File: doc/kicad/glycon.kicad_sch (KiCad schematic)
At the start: 17 parts, among them J1 2x20 Header, J2 USB_B, SW1 SW_Push, U0 Z80CPU, U1 628128_DIP32_SSOP32, U2 SST39SF010, U3 74HC32, U4 74HC86, X1 ACO-6.00MHz

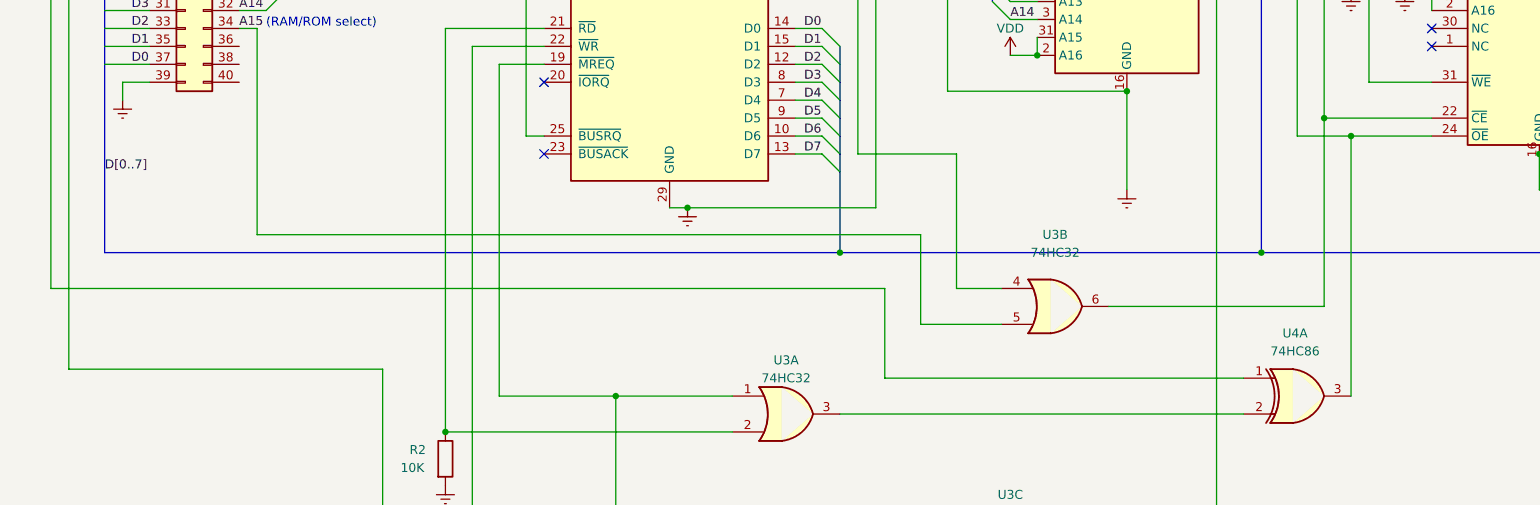
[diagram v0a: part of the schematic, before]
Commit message: add xor gates between coproc header and OE, ROM WE
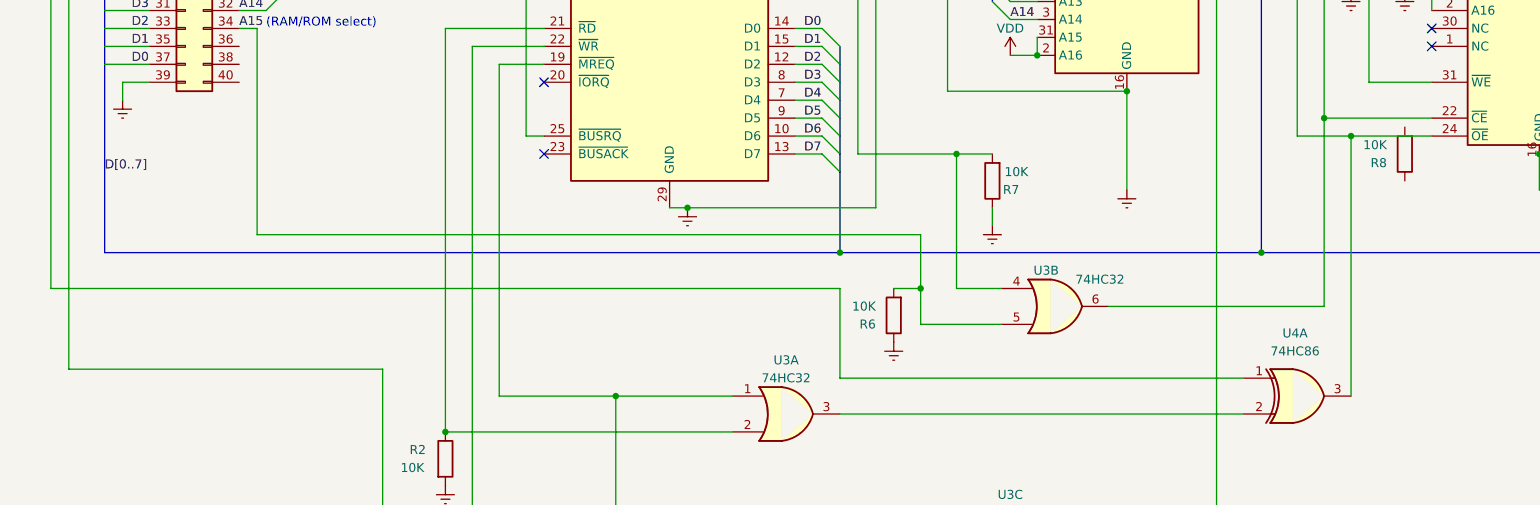
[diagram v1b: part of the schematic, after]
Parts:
- added R6, R7, R8: 10K, Resistor_THT:R_Axial_DIN0204_L3.6mm_D1.6mm_P5.08mm_Horizontal, symbol Device:R
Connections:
- net A15: now also R6.2
- net Earth: now also R6.1, R7.1
- net at U0.5 (A15), U3.4: now also R7.2
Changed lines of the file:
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@@
   (junction (at 114.3 114.3) (diameter 0) (color 0 0 0 0)
   )
+  (junction (at 147.32 125.73) (diameter 0) (color 0 0 0 0)
+  )
   (junction (at 111.76 38.1) (diameter 0) (color 0 0 0 0)
   )
@@
   )
   (junction (at 234.95 35.56) (diameter 0) (color 0 0 0 0)
+  )
+  (junction (at 152.4 106.68) (diameter 0) (color 0 0 0 0)
   )
   (junction (at 91.44 76.2) (diameter 0) (color 0 0 0 0)
@@
     (stroke (width 0) (type default) (color 0 0 0 0))
   )
-  (wire (pts (xy 147.32 118.11) (xy 147.32 130.81))
+  (wire (pts (xy 147.32 118.11) (xy 147.32 125.73))
     (stroke (width 0) (type default) (color 0 0 0 0))
   )
@@
     (stroke (width 0) (type default) (color 0 0 0 0))
   )
-  (wire (pts (xy 142.24 138.43) (xy 142.24 125.73))
+  (wire (pts (xy 135.89 138.43) (xy 135.89 125.73))
     (stroke (width 0) (type default) (color 0 0 0 0))
   )
@@
     (stroke (width 0) (type default) (color 0 0 0 0))
   )
-  (wire (pts (xy 193.04 138.43) (xy 142.24 138.43))
+  (wire (pts (xy 193.04 138.43) (xy 135.89 138.43))
     (stroke (width 0) (type default) (color 0 0 0 0))
   )
@@
     (stroke (width 0) (type default) (color 0 0 0 0))
   )
+  (wire (pts (xy 157.48 114.3) (xy 157.48 116.84))
+    (stroke (width 0) (type default) (color 0 0 0 0))
+  )
   (wire (pts (xy 250.19 63.5) (xy 254 63.5))
     (stroke (width 0) (type default) (color 0 0 0 0))
@@
     (stroke (width 0) (type default) (color 0 0 0 0))
   )
+  (wire (pts (xy 152.4 106.68) (xy 152.4 125.73))
+    (stroke (width 0) (type default) (color 0 0 0 0))
+  )
   (wire (pts (xy 160.02 80.01) (xy 163.83 80.01))
     (stroke (width 0) (type default) (color 0 0 0 0))
@@
     (stroke (width 0) (type default) (color 0 0 0 0))
   )
+  (wire (pts (xy 143.51 125.73) (xy 147.32 125.73))
+    (stroke (width 0) (type default) (color 0 0 0 0))
+  )
   (wire (pts (xy 91.44 60.96) (xy 93.98 60.96))
     (stroke (width 0) (type default) (color 0 0 0 0))
@@
     (stroke (width 0) (type default) (color 0 0 0 0))
   )
+  (wire (pts (xy 147.32 125.73) (xy 147.32 130.81))
+    (stroke (width 0) (type default) (color 0 0 0 0))
+  )
   (wire (pts (xy 50.8 86.36) (xy 54.61 86.36))
     (stroke (width 0) (type default) (color 0 0 0 0))
@@
     (stroke (width 0) (type default) (color 0 0 0 0))
   )
-  (wire (pts (xy 152.4 125.73) (xy 152.4 106.68))
-    (stroke (width 0) (type default) (color 0 0 0 0))
-  )
   (bus (pts (xy 57.15 73.66) (xy 57.15 76.2))
     (stroke (width 0) (type default) (color 0 0 0 0))
@@
     (stroke (width 0) (type default) (color 0 0 0 0))
   )
+  (wire (pts (xy 152.4 106.68) (xy 157.48 106.68))
+    (stroke (width 0) (type default) (color 0 0 0 0))
+  )
   (bus (pts (xy 213.36 55.88) (xy 213.36 53.34))
     (stroke (width 0) (type default) (color 0 0 0 0))
@@
     (stroke (width 0) (type default) (color 0 0 0 0))
   )
-  (wire (pts (xy 142.24 125.73) (xy 24.13 125.73))
+  (wire (pts (xy 135.89 125.73) (xy 24.13 125.73))
     (stroke (width 0) (type default) (color 0 0 0 0))
   )
@@
   (label "A13" (at 160.02 85.09 0)
     (effects (font (size 1.27 1.27)) (justify left bottom))
+  )
+  (symbol (lib_id "power:Earth") (at 157.48 116.84 0) (unit 1)
+    (in_bom yes) (on_board yes) (fields_autoplaced)
+    (property "Reference" "#PWR09" (id 0) (at 157.48 123.19 0)
+      (effects (font (size 1.27 1.27)) hide)
+    )
+    (property "Value" "Earth" (id 1) (at 157.48 120.65 0)
+      (effects (font (size 1.27 1.27)) hide)
+    )
+    (property "Footprint" "" (id 2) (at 157.48 116.84 0)
+      (effects (font (size 1.27 1.27)) hide)
+    )
+    (property "Datasheet" "~" (id 3) (at 157.48 116.84 0)
+      (effects (font (size 1.27 1.27)) hide)
+    )
+    (pin "1")
   )
   (symbol (lib_id "power:Earth") (at 41.91 187.96 0) (unit 1)
@@
     (pin "9")
   )
+  (symbol (lib_id "Device:R") (at 215.9 106.68 180) (unit 1)
+    (in_bom yes) (on_board yes)
+    (property "Reference" "R8" (id 0) (at 213.36 107.9501 0)
+      (effects (font (size 1.27 1.27)) (justify left))
+    )
+    (property "Value" "10K" (id 1) (at 213.36 105.41 0)
+      (effects (font (size 1.27 1.27)) (justify left))
+    )
+    (property "Footprint" "Resistor_THT:R_Axial_DIN0204_L3.6mm_D1.6mm_P5.08mm_Horizontal" (id 2) (at 217.678 106.68 90)
+      (effects (font (size 1.27 1.27)) hide)
+    )
+    (property "Datasheet" "~" (id 3) (at 215.9 106.68 0)
+      (effects (font (size 1.27 1.27)) hide)
+    )
+    (pin "1")
+    (pin "2")
+  )
   (symbol (lib_id "power:VDD") (at 34.29 26.67 0) (unit 1)
     (in_bom yes) (on_board yes) (fields_autoplaced)
@@
     )
     (pin "1")
+  )
+  (symbol (lib_id "Device:R") (at 143.51 129.54 180) (unit 1)
+    (in_bom yes) (on_board yes)
+    (property "Reference" "R6" (id 0) (at 140.97 130.8101 0)
+      (effects (font (size 1.27 1.27)) (justify left))
+    )
+    (property "Value" "10K" (id 1) (at 140.97 128.27 0)
+      (effects (font (size 1.27 1.27)) (justify left))
+    )
+    (property "Footprint" "Resistor_THT:R_Axial_DIN0204_L3.6mm_D1.6mm_P5.08mm_Horizontal" (id 2) (at 145.288 129.54 90)
+      (effects (font (size 1.27 1.27)) hide)
+    )
+    (property "Datasheet" "~" (id 3) (at 143.51 129.54 0)
+      (effects (font (size 1.27 1.27)) hide)
+    )
+    (pin "1")
+    (pin "2")
   )
   (symbol (lib_id "power:VDD") (at 160.02 92.71 0) (unit 1)
@@
     (pin "2")
   )
+  (symbol (lib_id "power:Earth") (at 143.51 133.35 0) (unit 1)
+    (in_bom yes) (on_board yes) (fields_autoplaced)
+    (property "Reference" "#PWR08" (id 0) (at 143.51 139.7 0)
+      (effects (font (size 1.27 1.27)) hide)
+    )
+    (property "Value" "Earth" (id 1) (at 143.51 137.16 0)
+      (effects (font (size 1.27 1.27)) hide)
+    )
+    (property "Footprint" "" (id 2) (at 143.51 133.35 0)
+      (effects (font (size 1.27 1.27)) hide)
+    )
+    (property "Datasheet" "~" (id 3) (at 143.51 133.35 0)
+      (effects (font (size 1.27 1.27)) hide)
+    )
+    (pin "1")
+  )
   (symbol (lib_id "power:VDD") (at 64.77 162.56 0) (unit 1)
     (in_bom yes) (on_board yes) (fields_autoplaced)
@@
   )
   (symbol (lib_id "74xx:74LS32") (at 166.37 128.27 0) (unit 2)
-    (in_bom yes) (on_board yes) (fields_autoplaced)
-    (property "Reference" "U3" (id 0) (at 166.37 118.11 0))
-    (property "Value" "74HC32" (id 1) (at 166.37 120.65 0))
+    (in_bom yes) (on_board yes)
+    (property "Reference" "U3" (id 0) (at 165.1 123.19 0))
+    (property "Value" "74HC32" (id 1) (at 172.72 124.46 0))
     (property "Footprint" "Package_DIP:DIP-14_W7.62mm_Socket" (id 2) (at 166.37 128.27 0)
       (effects (font (size 1.27 1.27)) hide)
@@
     (pin "1")
   )
+  (symbol (lib_id "Device:R") (at 157.48 110.49 180) (unit 1)
+    (in_bom yes) (on_board yes)
+    (property "Reference" "R7" (id 0) (at 161.29 111.76 0)
+      (effects (font (size 1.27 1.27)) (justify left))
+    )
+    (property "Value" "10K" (id 1) (at 162.56 109.22 0)
+      (effects (font (size 1.27 1.27)) (justify left))
+    )
+    (property "Footprint" "Resistor_THT:R_Axial_DIN0204_L3.6mm_D1.6mm_P5.08mm_Horizontal" (id 2) (at 159.258 110.49 90)
+      (effects (font (size 1.27 1.27)) hide)
+    )
+    (property "Datasheet" "~" (id 3) (at 157.48 110.49 0)
+      (effects (font (size 1.27 1.27)) hide)
+    )
+    (pin "1")
+    (pin "2")
+  )
   (symbol (lib_id "power:Earth") (at 208.28 83.82 0) (unit 1)
     (in_bom yes) (on_board yes) (fields_autoplaced)
@@
       (reference "#PWR07") (unit 1) (value "Earth") (footprint "")
     )
+    (path "/6ad14b56-675c-4a23-a7f2-ccda12e7dd3d"
+      (reference "#PWR08") (unit 1) (value "Earth") (footprint "")
+    )
+    (path "/02fc0791-5426-474d-b99e-2fa5261f57ec"
+      (reference "#PWR09") (unit 1) (value "Earth") (footprint "")
+    )
     (path "/e64349b4-ce91-4052-899d-02cb03ff264b"
       (reference "#PWR0101") (unit 1) (value "Earth") (footprint "")
@@
       (reference "R5") (unit 1) (value "10K") (footprint "Resistor_THT:R_Axial_DIN0204_L3.6mm_D1.6mm_P5.08mm_Horizontal")
     )
+    (path "/599a0f28-c99b-4bd8-870a-054e4f112491"
+      (reference "R6") (unit 1) (value "10K") (footprint "Resistor_THT:R_Axial_DIN0204_L3.6mm_D1.6mm_P5.08mm_Horizontal")
+    )
+    (path "/b3226ea6-3423-4308-90ad-d9ebe2611711"
+      (reference "R7") (unit 1) (value "10K") (footprint "Resistor_THT:R_Axial_DIN0204_L3.6mm_D1.6mm_P5.08mm_Horizontal")
+    )
+    (path "/5143db08-e7af-4d9c-98d0-1bce931f6e57"
+      (reference "R8") (unit 1) (value "10K") (footprint "Resistor_THT:R_Axial_DIN0204_L3.6mm_D1.6mm_P5.08mm_Horizontal")
+    )
     (path "/fd3d9773-922e-41cc-b486-19ed8a75f40a"
